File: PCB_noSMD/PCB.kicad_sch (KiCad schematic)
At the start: 7 parts, among them J10 Screw_Terminal_01x02, J4 Conn_01x12_Socket, J5 Conn_01x16_Socket, J6 Conn_01x08_Socket, J7 Conn_01x06_Socket, J8 Conn_01x08_Socket, J9 Screw_Terminal_01x02

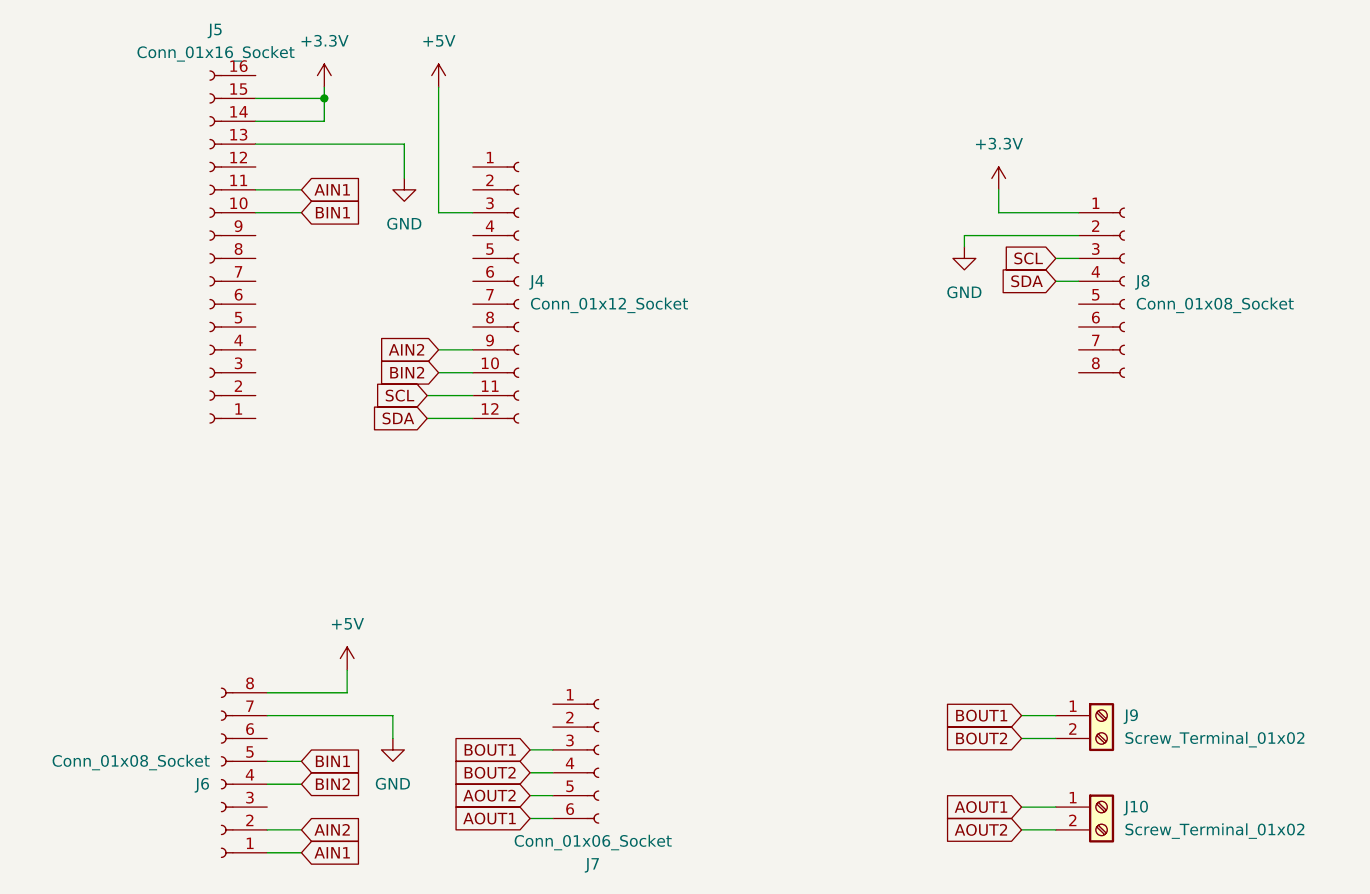
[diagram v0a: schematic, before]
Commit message: Finished 2nd PCB
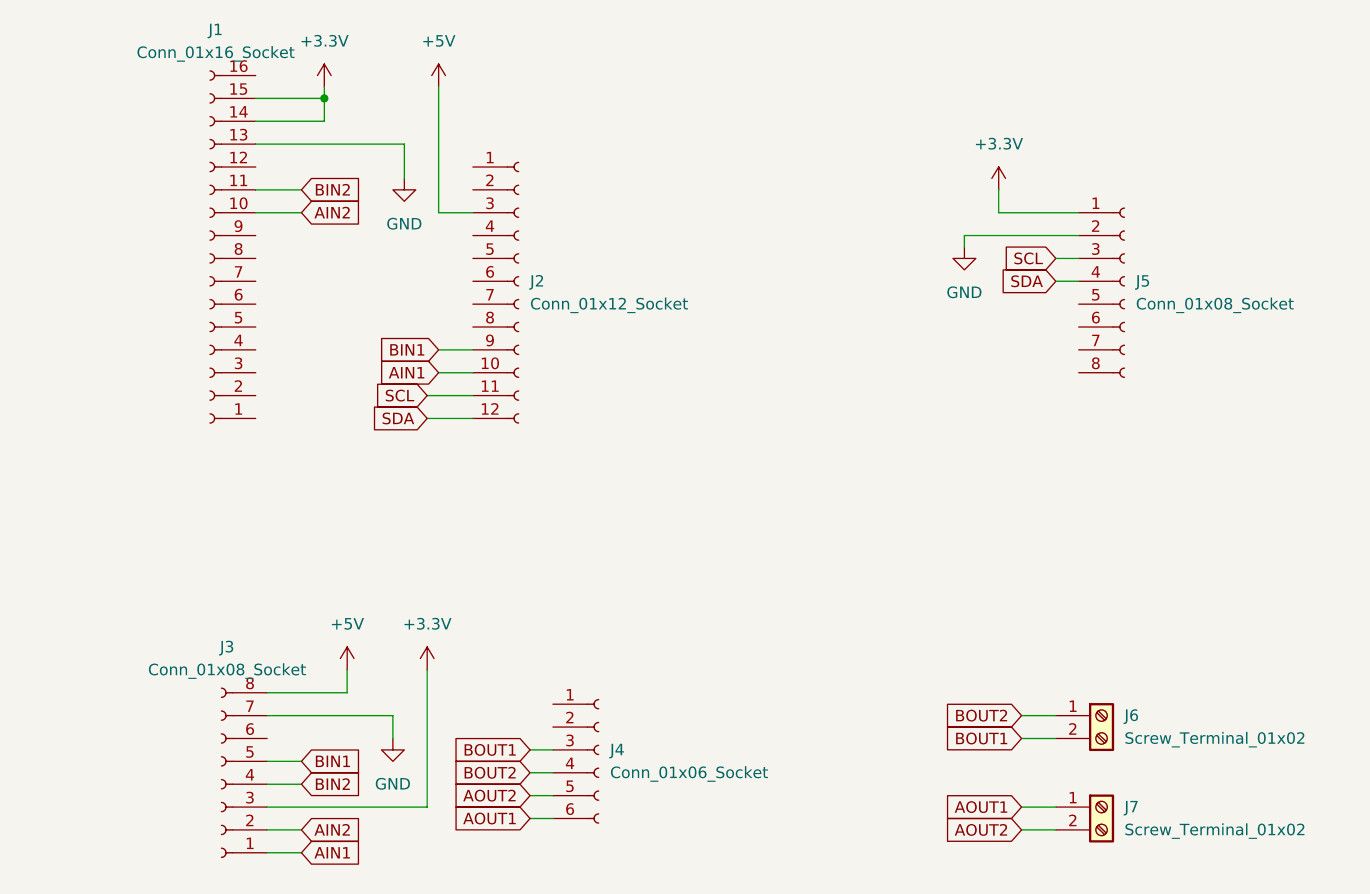
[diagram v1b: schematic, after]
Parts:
- J6: renamed from J9; footprint Connector_Phoenix_GMSTB:PhoenixContact_GMSTBA_2,5_2-G_1x02_P7.50mm_Horizontal -> Connector_PinHeader_2.54mm:PinHeader_1x02_P2.54mm_Vertical
- J7: renamed from J10; footprint Connector_Phoenix_GMSTB:PhoenixContact_GMSTBA_2,5_2-G_1x02_P7.50mm_Horizontal -> Connector_PinHeader_2.54mm:PinHeader_1x02_P2.54mm_Vertical
- renumbered J5 to J1, J4 to J2, J6 to J3, J7 to J4, J8 to J5
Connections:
- net +3.3V: now also J3.3 (Pin_3)
- net AIN1: now also J2.10 (Pin_10); no longer J1.11 (Pin_11)
- net AIN2: now also J1.10 (Pin_10); no longer J2.9 (Pin_9)
- net BIN1: now also J2.9 (Pin_9); no longer J1.10 (Pin_10)
- net BIN2: now also J1.11 (Pin_11); no longer J2.10 (Pin_10)
- net BOUT1: now also J6.2 (Pin_2); no longer J6.1 (Pin_1)
- net BOUT2: now also J6.1 (Pin_1); no longer J6.2 (Pin_2)
